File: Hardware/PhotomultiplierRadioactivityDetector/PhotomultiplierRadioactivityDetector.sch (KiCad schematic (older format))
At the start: 0 parts

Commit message: initial version rework
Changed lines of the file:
@@
 $Descr A4 11693 8268
 encoding utf-8
-Sheet 1 4
+Sheet 1 5
 Title ""
 Date ""
@@
 F1 "PhotompultiplierInputCircuit.sch" 50
 $EndSheet
+$Sheet
+S 4000 1950 500  150
+U 5EF1F288
+F0 "DataProcessing" 50
+F1 "DataProcessing.sch" 50
+$EndSheet
 $EndSCHEMATC

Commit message: draft of amplifier
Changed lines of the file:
@@
 $Descr A4 11693 8268
 encoding utf-8
-Sheet 1 5
+Sheet 1 6
 Title ""
 Date ""
@@
 $EndDescr
 $Sheet
-S 2500 1900 500  150
+S 3800 1900 500  150
 U 5EDA53F3
 F0 "DataAcquisition" 50
@@
 $EndSheet
 $Sheet
-S 4000 1950 500  150
+S 5300 1950 500  150
 U 5EF1F288
 F0 "DataProcessing" 50
 F1 "DataProcessing.sch" 50
 $EndSheet
+$Sheet
+S 2550 1950 500  150
+U 5EFA52FA
+F0 "Amplification" 50
+F1 "Amplification.sch" 50
+$EndSheet
 $EndSCHEMATC

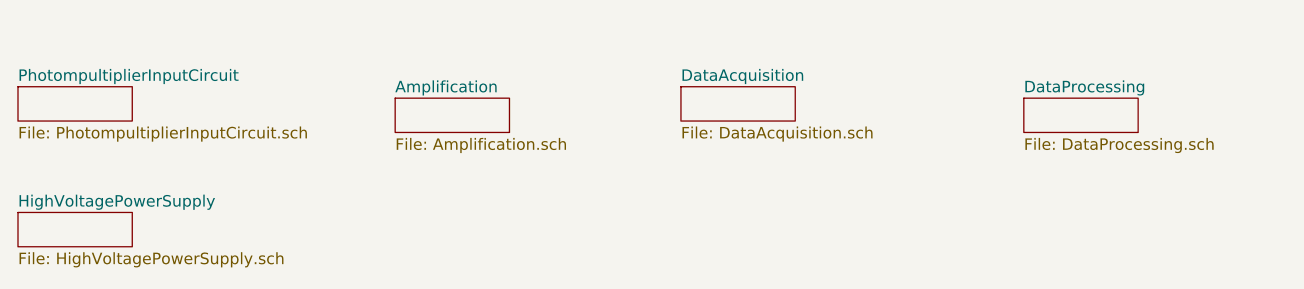
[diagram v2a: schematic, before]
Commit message: split for continous and pulse mode
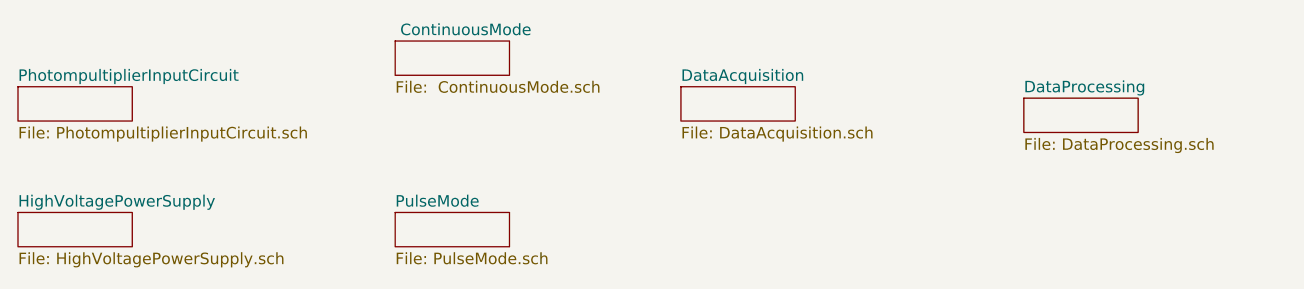
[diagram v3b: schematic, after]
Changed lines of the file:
@@
 $Descr A4 11693 8268
 encoding utf-8
-Sheet 1 6
+Sheet 1 7
 Title ""
 Date ""
@@
 $EndSheet
 $Sheet
-S 2550 1950 500  150
-U 5EFA52FA
-F0 "Amplification" 50
-F1 "Amplification.sch" 50
+S 2550 1700 500  150
+U 5EE61922
+F0 " ContinuousMode" 50
+F1 " ContinuousMode.sch" 50
+$EndSheet
+$Sheet
+S 2550 2450 500  150
+U 5EE9D63B
+F0 "PulseMode" 50
+F1 "PulseMode.sch" 50
 $EndSheet
 $EndSCHEMATC
